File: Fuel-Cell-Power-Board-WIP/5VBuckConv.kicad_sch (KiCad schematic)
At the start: 7 parts, among them U3 LM2576D2TR4-5G

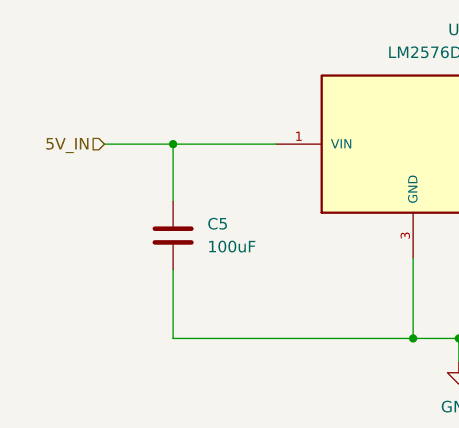
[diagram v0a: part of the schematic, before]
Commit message: made changes to Power flow stuff
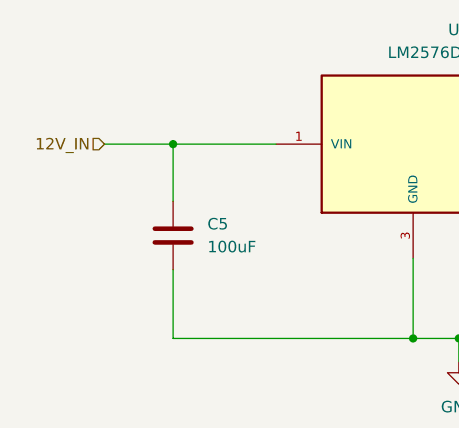
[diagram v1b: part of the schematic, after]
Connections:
- net 5V_IN renamed 12V_IN
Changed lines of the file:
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@@
     (effects (font (size 1.27 1.27)) (justify left))
   )
-  (hierarchical_label "5V_IN" (shape input) (at 52.07 88.9 180) (fields_autoplaced)
+  (hierarchical_label "12V_IN" (shape input) (at 52.07 88.9 180) (fields_autoplaced)
     (effects (font (size 1.27 1.27)) (justify right))
   )
